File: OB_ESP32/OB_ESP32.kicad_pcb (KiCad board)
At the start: 4 copper layers, 27.9 x 27.9 mm, 75 parts, among them J1 GPIOC, J2 GPIOA, J3 CAM, J4 GPIOB, J5 U.FL-R-SMT(01), U1 V3S, U2 EA3058, U3 WS2812-2020, U5 ESP32-PICO-D4, Y1 X1E0000210832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

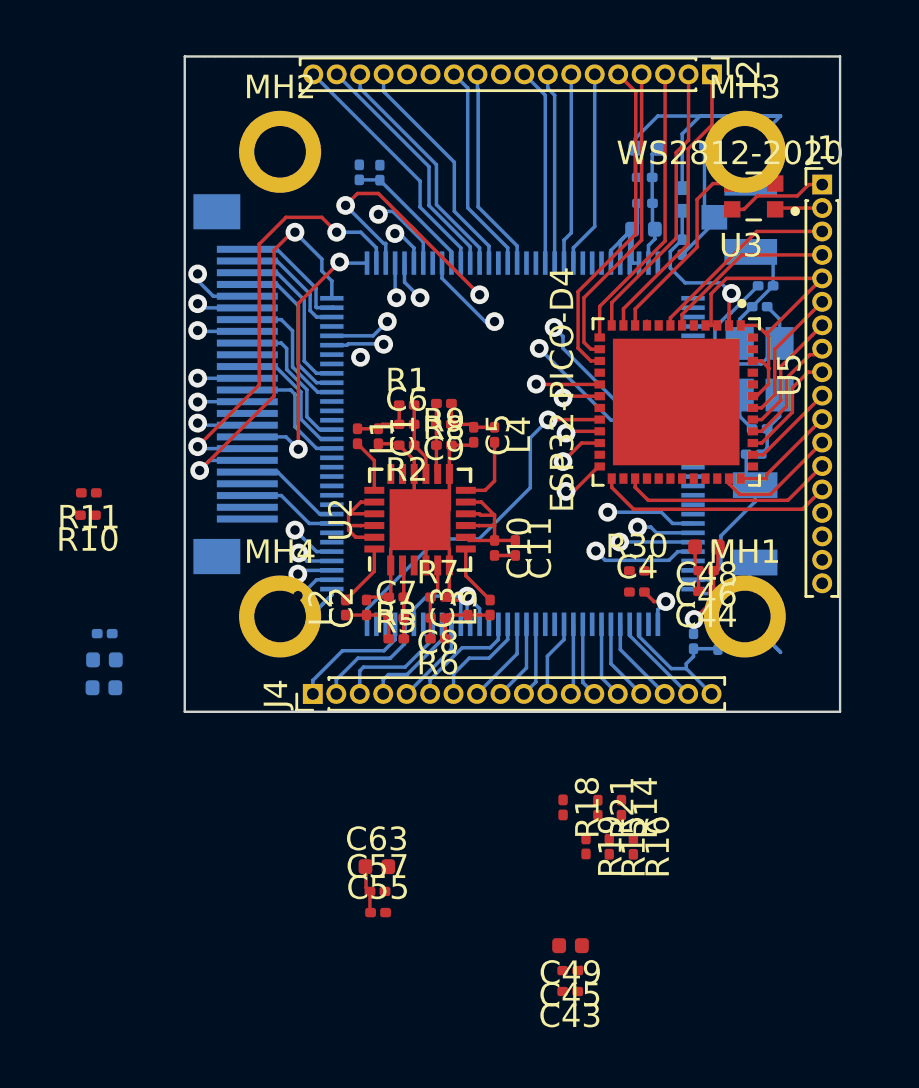
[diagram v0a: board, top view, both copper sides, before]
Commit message: mounting hole placement fix, routing allmost done
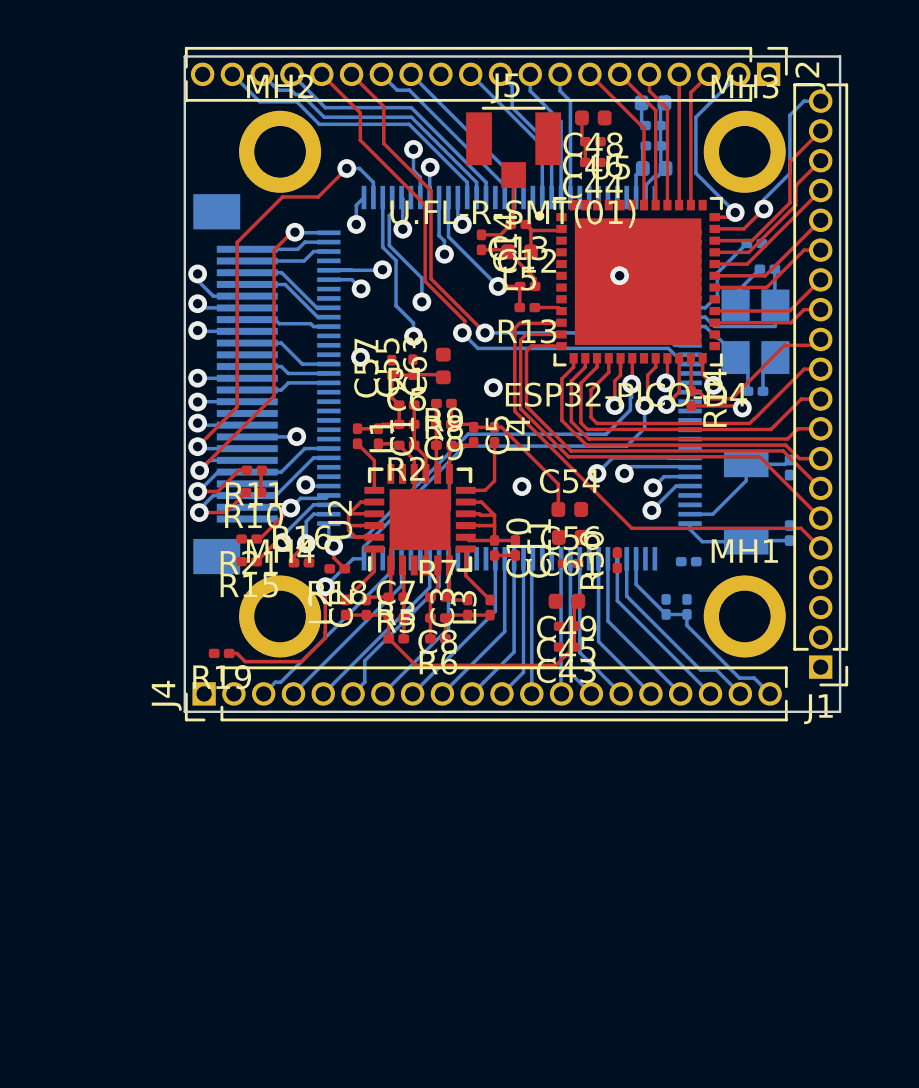
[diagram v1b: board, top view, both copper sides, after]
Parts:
- removed U3: WS2812-2020, WS2812-2020:LED_WS2812-2020
- C12, C13, C14, C54, C56, C61, J5, L5, R13: moved to F.Cu
- C4: moved to B.Cu
- J1, J2, J4: footprint Connector_PinHeader_1.00mm:PinHeader_1x18_P1.00mm_Vertical -> Connector_PinHeader_1.27mm:PinHeader_1x20_P1.27mm_Vertical
- moved C55 23.3 mm to (149.4, 89.4), turned to 90 degrees
- moved C57 22.3 mm to (148.5, 89.5), turned to 90 degrees
- moved C63 21.5 mm to (150.7, 89.4), turned to 90 degrees
- moved C54 21.3 mm to (156.1, 95.5)
- moved J1 20.6 mm to (166.8, 102.2), turned to 180 degrees
- moved C61 20.5 mm to (156.1, 96.7)
- moved C56 20.1 mm to (156.1, 97.8)
- moved R15 19.6 mm to (142.4, 97.7), turned to 180 degrees
- moved C44 18.9 mm to (157.1, 80.7)
- moved C46 18.9 mm to (157.1, 79.8)
- moved C48 18.9 mm to (157.1, 78.8)
- moved R21 18.8 mm to (142.4, 96.8), turned to 180 degrees
- moved R16 18.6 mm to (144.7, 97.8), turned to 0 degrees
- moved R14 17.7 mm to (161.3, 90.8)
- moved R19 17.6 mm to (141.3, 101.7), turned to 180 degrees
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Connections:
- J1 pad 1: +BATT -> EPHY_TX_P
- J1 pad 10: /WIFI, BT, RT/IO19 -> /WIFI, BT, RT/IO26
- J1 pad 11: /WIFI, BT, RT/IO23 -> /WIFI, BT, RT/IO27
- J1 pad 12: /WIFI, BT, RT/IO18 -> /WIFI, BT, RT/IO0
- J1 pad 14: /WIFI, BT, RT/IO16 -> /WIFI, BT, RT/SD2
- J1 pad 15: EPHY_RX_N -> /WIFI, BT, RT/CMD
- J1 pad 16: EPHY_RX_P -> /WIFI, BT, RT/CLK
- J1 pad 17: EPHY_TX_N -> /WIFI, BT, RT/SD0
- J1 pad 18: EPHY_TX_P -> /WIFI, BT, RT/SD1
- J1 pad 2: /WIFI, BT, RT/WS2812_DO -> EPHY_TX_N
- J1 pad 3: /WIFI, BT, RT/SENSOR_CAPN -> EPHY_RX_P
- J1 pad 4: /WIFI, BT, RT/SENSOR_CAPP -> EPHY_RX_N
- J1 pad 5: +3V3 -> /WIFI, BT, RT/IO34
- J1 pad 6: /WIFI, BT, RT/IO42 -> /WIFI, BT, RT/IO35
- J1 pad 7: /WIFI, BT, RT/UART0_TX -> /WIFI, BT, RT/IO32
- J1 pad 8: /WIFI, BT, RT/UART0_RX -> /WIFI, BT, RT/IO33
- J1 pad 9: /WIFI, BT, RT/IO22 -> /WIFI, BT, RT/IO25
- J2 pad 1: IO35 -> GND
- J2 pad 10: GND -> /All V3s input output/SPI_CLK
- J2 pad 11: /All V3s input output/UART0_TX -> /All V3s input output/SPI_MISO
- J2 pad 12: /All V3s input output/UART0_RX -> GND
- J2 pad 13: /All V3s input output/EPHY_LINK_LED -> /All V3s input output/UART0_TX
- J2 pad 14: /All V3s input output/EPHY_SPD_LED -> /All V3s input output/UART0_RX
- J2 pad 15: /All V3s input output/I2C0_SDA -> /All V3s input output/EPHY_LINK_LED
- J2 pad 16: /All V3s input output/I2C0_CLK -> /All V3s input output/EPHY_SPD_LED
- J2 pad 17: /All V3s input output/PB5 -> /All V3s input output/I2C0_SDA
- J2 pad 18: /All V3s input output/PB4 -> /All V3s input output/I2C0_CLK
- J2 pad 2: IO33 -> IO23
- J2 pad 3: IO32 -> IO19
- J2 pad 4: IO25 -> IO22
- J2 pad 5: IO26 -> /WIFI, BT, RT/UART0_RX
- J2 pad 6: /All V3s input output/SPI_MOSI -> /WIFI, BT, RT/UART0_TX
- J2 pad 7: /All V3s input output/SPI_CS -> IO21
- J2 pad 8: /All V3s input output/SPI_CLK -> /All V3s input output/SPI_MOSI
- J2 pad 9: /All V3s input output/SPI_MISO -> /All V3s input output/SPI_CS
- J4 pad 1: /All V3s input output/HPCOM -> +BATT
- J4 pad 10: /All V3s input output/USB_D_N -> /All V3s input output/LRDAC0
- J4 pad 11: /All V3s input output/PF0 -> /All V3s input output/USB_D_P
- J4 pad 12: /All V3s input output/PF1 -> /All V3s input output/USB_D_N
- J4 pad 13: /All V3s input output/PF2 -> /All V3s input output/PF0
- J4 pad 14: /All V3s input output/PF3 -> /All V3s input output/PF1
- J4 pad 15: /All V3s input output/PF4 -> /All V3s input output/PF2
- J4 pad 16: /All V3s input output/PF5 -> /All V3s input output/PF3
- J4 pad 17: /All V3s input output/USB_ID -> /All V3s input output/PF4
- J4 pad 18: /All V3s input output/RST -> /All V3s input output/PF5
- J4 pad 2: /All V3s input output/HPCOMFB -> GND
- J4 pad 3: /All V3s input output/HPOUTL -> /All V3s input output/HPCOM
- J4 pad 4: /All V3s input output/HPOUTR -> /All V3s input output/HPCOMFB
- J4 pad 5: /All V3s input output/HBIAS -> /All V3s input output/HPOUTL
- J4 pad 6: /All V3s input output/MICIN1N -> /All V3s input output/HPOUTR
- J4 pad 7: /All V3s input output/MICIN1P -> /All V3s input output/HBIAS
- J4 pad 8: /All V3s input output/LRDAC0 -> /All V3s input output/MICIN1N
- J4 pad 9: /All V3s input output/USB_D_P -> /All V3s input output/MICIN1P
- U5 pad 10: /WIFI, BT, RT/WS2812_DI -> /WIFI, BT, RT/IO34
- U5 pad 11: IO35 -> /WIFI, BT, RT/IO35
- U5 pad 12: IO33 -> /WIFI, BT, RT/IO32
- U5 pad 13: IO32 -> /WIFI, BT, RT/IO33
- U5 pad 14: IO25 -> /WIFI, BT, RT/IO25
- U5 pad 15: IO26 -> /WIFI, BT, RT/IO26
- U5 pad 16: (no net) -> /WIFI, BT, RT/IO27
- U5 pad 25: /WIFI, BT, RT/IO16 -> (no net)
- U5 pad 28: (no net) -> /WIFI, BT, RT/SD2
- U5 pad 30: (no net) -> /WIFI, BT, RT/CMD
- U5 pad 31: (no net) -> /WIFI, BT, RT/CLK
- U5 pad 32: (no net) -> /WIFI, BT, RT/SD0
- U5 pad 33: (no net) -> /WIFI, BT, RT/SD1
- U5 pad 34: (no net) -> /WIFI, BT, RT/IO5
- U5 pad 36: /WIFI, BT, RT/IO23 -> IO23
- U5 pad 38: /WIFI, BT, RT/IO19 -> IO19
- U5 pad 39: /WIFI, BT, RT/IO22 -> IO22
- U5 pad 42: /WIFI, BT, RT/IO42 -> IO21
- U5 pad 6: /WIFI, BT, RT/SENSOR_CAPP -> (no net)
- U5 pad 7: /WIFI, BT, RT/SENSOR_CAPN -> (no net)
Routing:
- net GND: track 83.7 -> 30.7 mm, vias 1 -> 3
- net /WIFI, BT, RT/IO34: track 0.00 -> 21.1 mm
- net /WIFI, BT, RT/IO35: track 0.00 -> 19.5 mm
- net /WIFI, BT, RT/IO32: track 0.00 -> 17.9 mm
- net /WIFI, BT, RT/IO0_PULL: track 3.65 -> 21.2 mm, vias 1 -> 2
- net +3V3: track 22.7 -> 7.59 mm, vias 1 -> 0
- net /WIFI, BT, RT/IO33: track 0.00 -> 14.6 mm
- net IO26: track 14.2 -> 0.00 mm
- net /WIFI, BT, RT/IO25: track 0.00 -> 14.1 mm
- net /WIFI, BT, RT/IO26: track 0.00 -> 13.9 mm
- net /WIFI, BT, RT/IO27: track 0.00 -> 13.7 mm
- net IO25: track 13.2 -> 0.00 mm
- net IO32: track 12.4 -> 0.00 mm
- net IO35: track 12.3 -> 0.00 mm
- net IO33: track 12.1 -> 0.00 mm
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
